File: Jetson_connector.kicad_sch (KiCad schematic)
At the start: 24 parts, among them IC2 AT24MAC402-MAHM-T, IC6 SN74AVC1T45DCKT, J2 QTH-060-01-L-D-A, U2 SN74AVC2T45DCUR

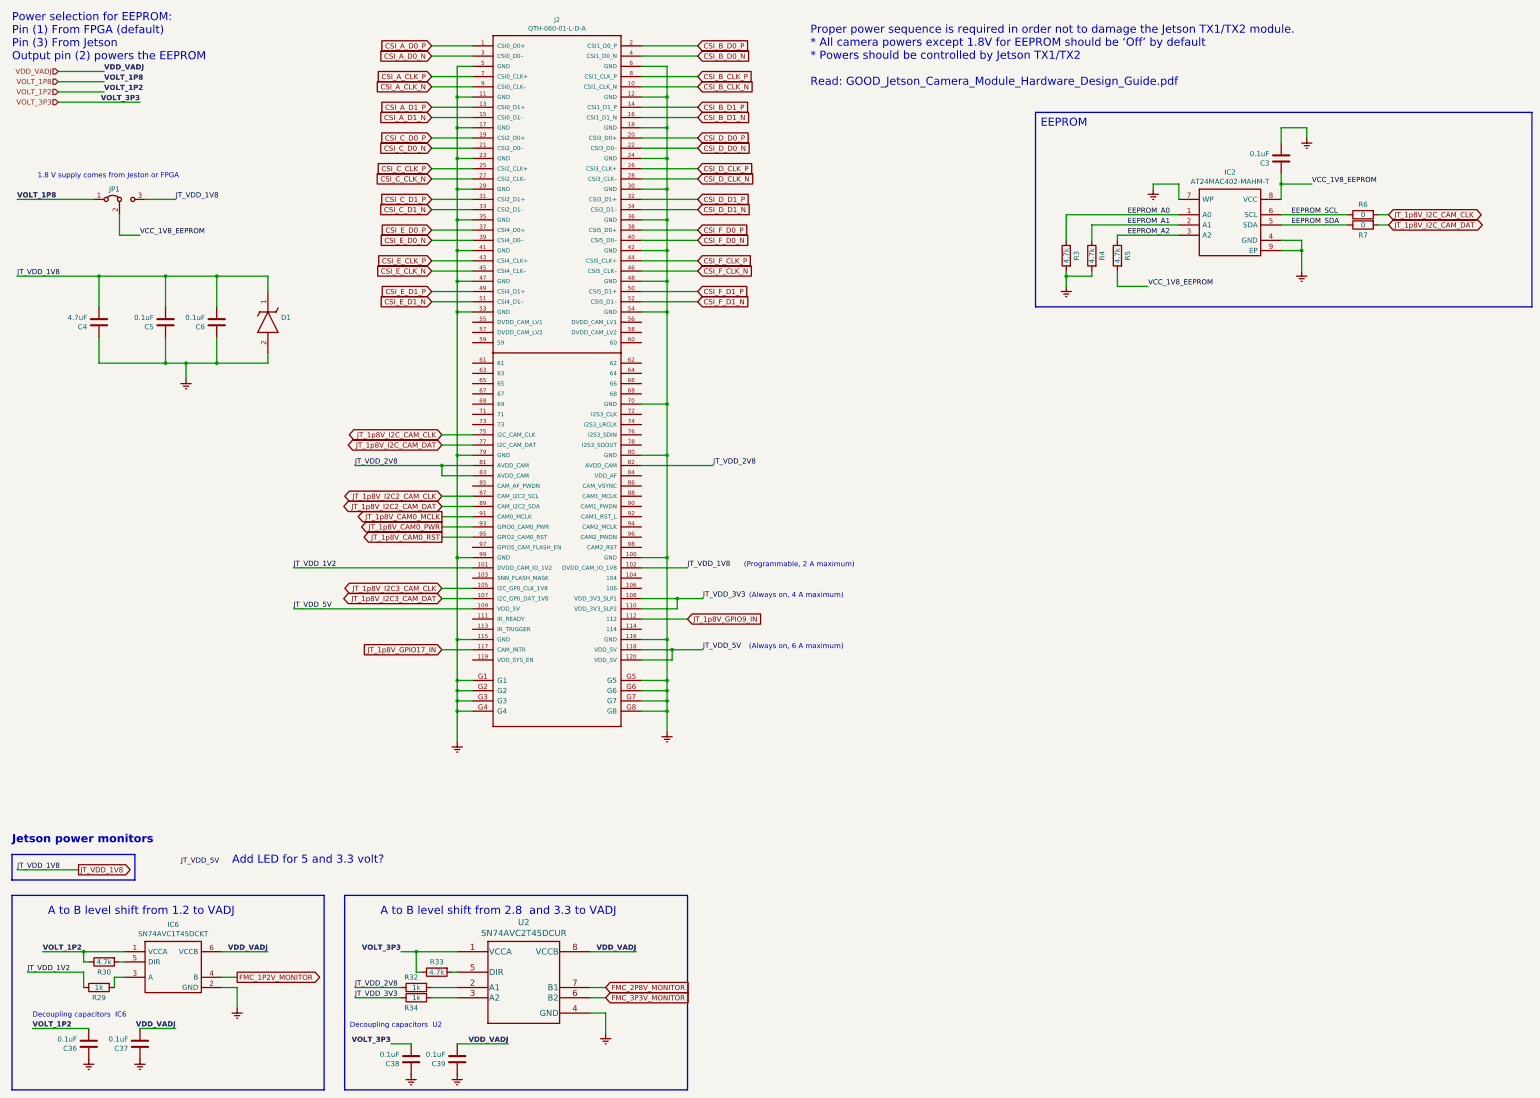
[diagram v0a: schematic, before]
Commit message: DRC, ERC OK
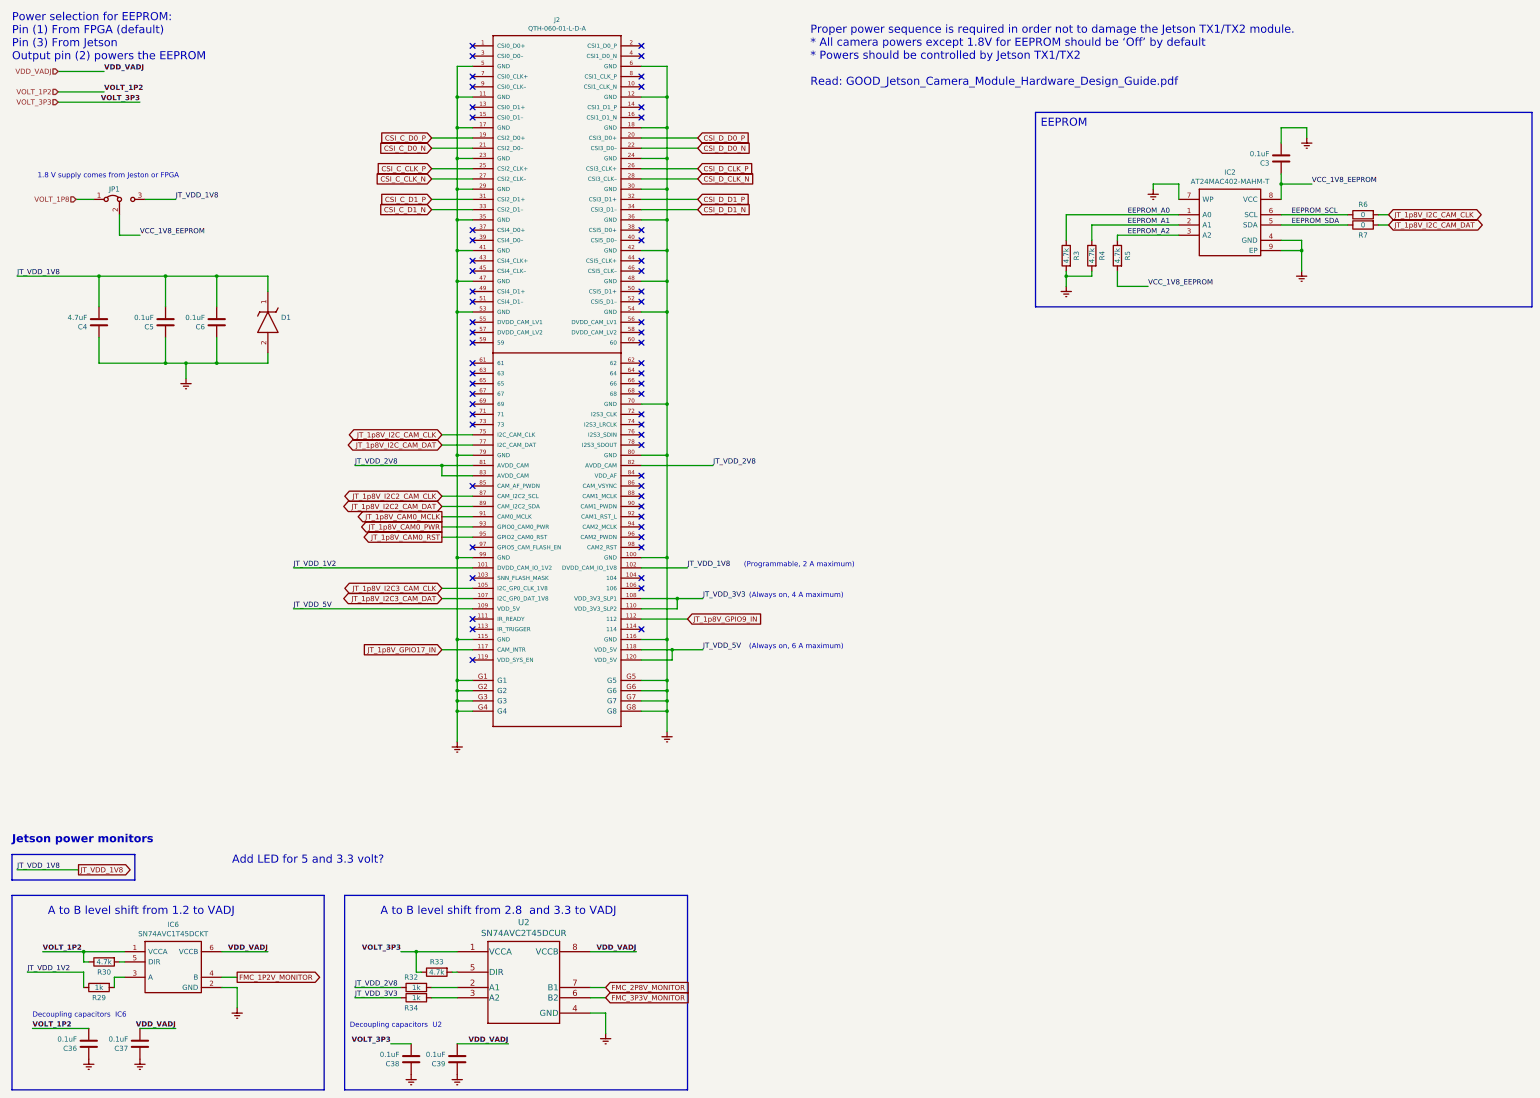
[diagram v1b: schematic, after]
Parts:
- D1: footprint Diodes_SMD:D_SOD-523 -> SODFL1608X70N
- IC6: footprint FMC_MIPI_v2_sym:SOT65P210X110-6N -> SOT65P210X110-6N
- JP1: symbol FMC_MIPI_v2-rescue:Jumper_3_Bridged12-Jumper -> FMC_MIPI_v2:Jumper_3_Bridged12-Jumper
- R29, R3, R30, R32, R33, R34, R4, R5, R6, R7: symbol FMC_MIPI_v2-rescue:R-Device -> FMC_MIPI_v2:R
- U2: footprint FMC_MIPI_v2_sym:SN74AVC2T45DCUR -> DCU8
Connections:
- net CSI_A_CLK_N: no longer names the net of J2.9 (CSI0_CLK–)
- net CSI_A_CLK_P: no longer names the net of J2.7 (CSI0_CLK+)
- net CSI_A_D0_N: no longer names the net of J2.3 (CSI0_D0–)
- net CSI_A_D0_P: no longer names the net of J2.1 (CSI0_D0+)
- net CSI_A_D1_N: no longer names the net of J2.15 (CSI0_D1–)
- net CSI_A_D1_P: no longer names the net of J2.13 (CSI0_D1+)
- net CSI_B_CLK_N: no longer names the net of J2.10 (CSI1_CLK_N)
- net CSI_B_CLK_P: no longer names the net of J2.8 (CSI1_CLK_P)
- net CSI_B_D0_N: no longer names the net of J2.4 (CSI1_D0_N)
- net CSI_B_D0_P: no longer names the net of J2.2 (CSI1_D0_P)
- net CSI_B_D1_N: no longer names the net of J2.16 (CSI1_D1_N)
- net CSI_B_D1_P: no longer names the net of J2.14 (CSI1_D1_P)
- net CSI_E_CLK_N: no longer names the net of J2.45 (CSI4_CLK–)
- net CSI_E_CLK_P: no longer names the net of J2.43 (CSI4_CLK+)
- net CSI_E_D0_N: no longer names the net of J2.39 (CSI4_D0–)
- net CSI_E_D0_P: no longer names the net of J2.37 (CSI4_D0+)
- net CSI_E_D1_N: no longer names the net of J2.51 (CSI4_D1–)
- net CSI_E_D1_P: no longer names the net of J2.49 (CSI4_D1+)
- net CSI_F_CLK_N: no longer names the net of J2.46 (CSI5_CLK–)
- net CSI_F_CLK_P: no longer names the net of J2.44 (CSI5_CLK+)
- net CSI_F_D0_N: no longer names the net of J2.40 (CSI5_D0–)
- net CSI_F_D0_P: no longer names the net of J2.38 (CSI5_D0+)
- net CSI_F_D1_N: no longer names the net of J2.52 (CSI5_D1–)
- net CSI_F_D1_P: no longer names the net of J2.50 (CSI5_D1+)
- removed net Earth: C3.2, C36.1, C37.1, C38.1, C39.1, C4.1, C5.1, C6.1, D1.2, IC2.4 (GND), IC2.7 (WP), IC2.9 (EP), IC6.2 (GND), J2.100 (GND), J2.11 (GND), J2.115 (GND), J2.116 (GND), J2.12 (GND), J2.17 (GND), J2.18 (GND), J2.23 (GND), J2.24 (GND), J2.29 (GND), J2.30 (GND), J2.35 (GND), J2.36 (GND), J2.41 (GND), J2.42 (GND), J2.47 (GND), J2.48 (GND), J2.5 (GND), J2.53 (GND), J2.54 (GND), J2.6 (GND), J2.70 (GND), J2.79 (GND), J2.80 (GND), J2.99 (GND), J2.G1, J2.G2, J2.G3, J2.G4, J2.G5, J2.G6, J2.G7, J2.G8, R3.2, R4.2, U2.4 (GND)
- new net: J2.100 (GND), J2.116 (GND), J2.12 (GND), J2.18 (GND), J2.24 (GND), J2.30 (GND), J2.36 (GND), J2.42 (GND), J2.48 (GND), J2.54 (GND), J2.6 (GND), J2.70 (GND), J2.80 (GND), J2.G5, J2.G6, J2.G7, J2.G8
- new net: J2.11 (GND), J2.115 (GND), J2.17 (GND), J2.23 (GND), J2.29 (GND), J2.35 (GND), J2.41 (GND), J2.47 (GND), J2.5 (GND), J2.53 (GND), J2.79 (GND), J2.99 (GND), J2.G1, J2.G2, J2.G3, J2.G4
- new net: C4.1, C5.1, C6.1, D1.2
- new net: IC2.4 (GND), IC2.9 (EP)
- new net: R3.2, R4.2
- no-connect marks 0 -> 62

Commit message: All warnings fixed
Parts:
- U2: footprint DCU8 -> FMC_MIPI_v2_sym:SN74AVC2T45DCUR
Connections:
- net Earth: now reaches J2.100 (GND), J2.116 (GND), J2.12 (GND), J2.18 (GND), J2.24 (GND), J2.30 (GND), J2.36 (GND), J2.42 (GND), J2.48 (GND), J2.54 (GND), J2.6 (GND), J2.70 (GND), J2.80 (GND), J2.G5, J2.G6, J2.G7, J2.G8
- net Earth: now also C3.2, C36.1, C37.1, C38.1, C39.1, C4.1, C5.1, C6.1, D1.2, IC2.4 (GND), IC2.7 (WP), IC2.9 (EP), IC6.2 (GND), J2.11 (GND), J2.115 (GND), J2.17 (GND), J2.23 (GND), J2.29 (GND), J2.35 (GND), J2.41 (GND), J2.47 (GND), J2.5 (GND), J2.53 (GND), J2.79 (GND), J2.99 (GND), J2.G1, J2.G2, J2.G3, J2.G4, R3.2, R4.2, U2.4 (GND)
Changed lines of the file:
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@@
       (effects (font (size 1.524 1.524)))
     )
-    (property "Footprint" "DCU8" (id 2) (at 142.24 242.57 0)
+    (property "Footprint" "FMC_MIPI_v2_sym:SN74AVC2T45DCUR" (id 2) (at 142.24 242.57 0)
       (effects (font (size 1.524 1.524)) hide)
     )

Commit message: JLCPCB BOM OK
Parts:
- C3, C36, C37, C38, C39, C5, C6: LCSC (none) -> C1525
- C4: LCSC (none) -> C1779; Part Number C2012X7R1H475K125AC -> CL21A475KAQNNNE
- D1: LCSC (none) -> C117557
- IC2, IC6, J2: LCSC (none) -> NeedToAsk
- JP1: LCSC (none) -> DnP; Part Number (none) -> 22-28-4033
- R29, R32, R34: value 1k -> 2.2k; LCSC (none) -> C17520; Part Number CRCW08051K00FKEAC -> (none)
- R3, R4, R5: LCSC (none) -> C17673
- R6, R7: LCSC (none) -> C17477; Part Number RC0805JR-070RL -> 0805W8F0000T5E
- U2: LCSC (none) -> C140318
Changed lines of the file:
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@@
       (effects (font (size 1.524 1.524)) hide)
+    )
+    (property "LCSC" "NeedToAsk" (id 4) (at 143.51 97.79 0)
+      (effects (font (size 1.27 1.27)) hide)
     )
     (pin "1")
@@
       (effects (font (size 1.27 1.27)) hide)
     )
-    (property "Datasheet" "~" (id 3) (at 41.91 59.69 0)
+    (property "Datasheet" "https://www.mouser.com/ProductDetail/Molex/22-28-4033?qs=d9fIA1aNikRRpuevshfBIQ%3D%3D" (id 3) (at 41.91 59.69 0)
+      (effects (font (size 1.27 1.27)) hide)
+    )
+    (property "Part Number" "22-28-4033" (id 4) (at 41.91 59.69 0)
+      (effects (font (size 1.27 1.27)) hide)
+    )
+    (property "LCSC" "DnP" (id 5) (at 41.91 59.69 0)
       (effects (font (size 1.27 1.27)) hide)
     )
@@
     (property "Manufacturer_Part_Number" "UCLAMP0501H.TCT" (id 9) (at 64.77 92.71 0)
       (effects (font (size 1.27 1.27)) (justify left bottom) hide)
+    )
+    (property "LCSC" "C117557" (id 10) (at 78.74 82.55 90)
+      (effects (font (size 1.27 1.27)) hide)
     )
     (pin "1")
@@
     (property "Manufacturer_Part_Number" "AT24MAC402-MAHM-T" (id 9) (at 326.39 73.66 0)
       (effects (font (size 1.27 1.27)) (justify left) hide)
+    )
+    (property "LCSC" "NeedToAsk" (id 10) (at 304.8 58.42 0)
+      (effects (font (size 1.27 1.27)) hide)
     )
     (pin "1")
@@
       (effects (font (size 1.27 1.27)) hide)
     )
+    (property "LCSC" "C1525" (id 7) (at 66.04 90.17 0)
+      (effects (font (size 1.27 1.27)) hide)
+    )
     (pin "1")
     (pin "2")
@@
       (effects (font (size 1.27 1.27)) hide)
     )
+    (property "LCSC" "C1525" (id 7) (at 53.34 90.17 0)
+      (effects (font (size 1.27 1.27)) hide)
+    )
     (pin "1")
     (pin "2")
@@
       (effects (font (size 1.27 1.27)) hide)
     )
-    (property "Datasheet" "https://www.mouser.com/ProductDetail/TDK/C2012X7R1H475K125AC?qs=P1JMDcb91o6brNyz9C%252BI3w%3D%3D" (id 3) (at 36.83 90.17 0)
-      (effects (font (size 1.27 1.27)) hide)
-    )
-    (property "Part Number" "C2012X7R1H475K125AC" (id 4) (at 36.83 90.17 0)
+    (property "Datasheet" "https://www.mouser.com/ProductDetail/Samsung-Electro-Mechanics/CL21A475KAQNNNE?qs=yOVawPpwOwkWIBpK%2Fbg0Aw%3D%3D" (id 3) (at 36.83 90.17 0)
+      (effects (font (size 1.27 1.27)) hide)
+    )
+    (property "Part Number" "CL21A475KAQNNNE" (id 4) (at 36.83 90.17 0)
       (effects (font (size 1.27 1.27)) hide)
     )
@@
     )
     (property "Voltage" "25V" (id 6) (at 36.83 90.17 0)
+      (effects (font (size 1.27 1.27)) hide)
+    )
+    (property "LCSC" "C1779" (id 7) (at 36.83 90.17 0)
       (effects (font (size 1.27 1.27)) hide)
     )
@@
       (effects (font (size 1.27 1.27)) hide)
     )
-    (property "Datasheet" "https://www.mouser.com/ProductDetail/YAGEO/RC0805JR-070RL?qs=3ldFlDWnkKyEhdaPjQHEFA%3D%3D" (id 3) (at 350.52 63.5 0)
+    (property "Datasheet" "https://www.mouser.com/ProductDetail/Royalohm/0805W8F0000T5E?qs=e8oIoAS2J1TZ0ecBNS6tzg%3D%3D" (id 3) (at 350.52 63.5 0)
       (effects (font (size 1.27 1.27)) hide)
     )
@@
       (effects (font (size 1.524 1.524)) hide)
     )
-    (property "Part Number" "RC0805JR-070RL" (id 6) (at 350.52 63.5 90)
-      (effects (font (size 1.524 1.524)) hide)
+    (property "Part Number" "0805W8F0000T5E" (id 6) (at 350.52 63.5 90)
+      (effects (font (size 1.524 1.524)) hide)
+    )
+    (property "LCSC" "C17477" (id 7) (at 388.62 198.12 90)
+      (effects (font (size 1.27 1.27)) hide)
     )
     (pin "1")
@@
       (effects (font (size 1.27 1.27)) hide)
     )
-    (property "Datasheet" "https://www.mouser.com/ProductDetail/YAGEO/RC0805JR-070RL?qs=3ldFlDWnkKyEhdaPjQHEFA%3D%3D" (id 3) (at 350.52 66.04 0)
+    (property "Datasheet" "https://www.mouser.com/ProductDetail/Royalohm/0805W8F0000T5E?qs=e8oIoAS2J1TZ0ecBNS6tzg%3D%3D" (id 3) (at 350.52 66.04 0)
       (effects (font (size 1.27 1.27)) hide)
     )
@@
       (effects (font (size 1.524 1.524)) hide)
     )
-    (property "Part Number" "RC0805JR-070RL" (id 6) (at 350.52 66.04 90)
-      (effects (font (size 1.524 1.524)) hide)
+    (property "Part Number" "0805W8F0000T5E" (id 6) (at 350.52 66.04 90)
+      (effects (font (size 1.524 1.524)) hide)
+    )
+    (property "LCSC" "C17477" (id 7) (at 388.62 198.12 90)
+      (effects (font (size 1.27 1.27)) hide)
     )
     (pin "1")
@@
     )
     (property "Voltage" "25V" (id 6) (at 330.2 49.53 0)
+      (effects (font (size 1.27 1.27)) hide)
+    )
+    (property "LCSC" "C1525" (id 7) (at 330.2 49.53 0)
       (effects (font (size 1.27 1.27)) hide)
     )
@@
       (effects (font (size 1.524 1.524)) hide)
     )
+    (property "LCSC" "C17673" (id 7) (at 276.86 73.66 90)
+      (effects (font (size 1.27 1.27)) hide)
+    )
     (pin "1")
     (pin "2")
@@
       (effects (font (size 1.524 1.524)) hide)
     )
+    (property "LCSC" "C17673" (id 7) (at 283.21 73.66 90)
+      (effects (font (size 1.27 1.27)) hide)
+    )
     (pin "1")
     (pin "2")
@@
       (effects (font (size 1.524 1.524)) hide)
     )
+    (property "LCSC" "C17673" (id 7) (at 289.56 73.66 90)
+      (effects (font (size 1.27 1.27)) hide)
+    )
     (pin "1")
     (pin "2")
@@
     (property "Manufacturer_Part_Number" "SN74AVC1T45DCKT" (id 9) (at 63.5 261.62 0)
       (effects (font (size 1.27 1.27)) (justify left) hide)
+    )
+    (property "LCSC" "NeedToAsk" (id 10) (at 39.37 246.38 0)
+      (effects (font (size 1.27 1.27)) hide)
     )
     (pin "1")
@@
     (in_bom yes) (on_board yes)
     (property "Reference" "R29" (id 0) (at 36.83 257.81 90))
-    (property "Value" "1k" (id 1) (at 36.83 255.27 90))
+    (property "Value" "2.2k" (id 1) (at 36.83 255.27 90))
     (property "Footprint" "Resistors_SMD:R_0805" (id 2) (at 36.83 253.492 90)
       (effects (font (size 1.27 1.27)) hide)
     )
-    (property "Datasheet" "https://www.mouser.com/ProductDetail/Vishay-Dale/CRCW08051K00FKEAC?qs=CZ6xfwOSLTXmQIgaYvN%2FBA%3D%3D" (id 3) (at 36.83 255.27 0)
+    (property "Datasheet" "" (id 3) (at 36.83 255.27 0)
       (effects (font (size 1.27 1.27)) hide)
     )
@@
       (effects (font (size 1.524 1.524)) hide)
     )
-    (property "Part Number" "CRCW08051K00FKEAC" (id 6) (at 36.83 255.27 90)
-      (effects (font (size 1.524 1.524)) hide)
+    (property "Part Number" "" (id 6) (at 36.83 255.27 90)
+      (effects (font (size 1.524 1.524)) hide)
+    )
+    (property "LCSC" "C17520" (id 7) (at 36.83 255.27 90)
+      (effects (font (size 1.27 1.27)) hide)
     )
     (pin "1")
@@
       (effects (font (size 1.27 1.27)) hide)
     )
+    (property "LCSC" "C1525" (id 7) (at 66.04 90.17 0)
+      (effects (font (size 1.27 1.27)) hide)
+    )
     (pin "1")
     (pin "2")
@@
     )
     (property "Voltage" "25V" (id 6) (at 46.99 269.24 0)
+      (effects (font (size 1.27 1.27)) hide)
+    )
+    (property "LCSC" "C1525" (id 7) (at 66.04 90.17 0)
       (effects (font (size 1.27 1.27)) hide)
     )
@@
     (in_bom yes) (on_board yes)
     (property "Reference" "R32" (id 0) (at 114.3 252.73 90))
-    (property "Value" "1k" (id 1) (at 115.57 255.27 90))
+    (property "Value" "2.2k" (id 1) (at 115.57 255.27 90))
     (property "Footprint" "Resistors_SMD:R_0805" (id 2) (at 115.57 253.492 90)
       (effects (font (size 1.27 1.27)) hide)
     )
-    (property "Datasheet" "https://www.mouser.com/ProductDetail/Vishay-Dale/CRCW08051K00FKEAC?qs=CZ6xfwOSLTXmQIgaYvN%2FBA%3D%3D" (id 3) (at 115.57 255.27 0)
+    (property "Datasheet" "" (id 3) (at 115.57 255.27 0)
       (effects (font (size 1.27 1.27)) hide)
     )
@@
       (effects (font (size 1.524 1.524)) hide)
     )
-    (property "Part Number" "CRCW08051K00FKEAC" (id 6) (at 115.57 255.27 90)
-      (effects (font (size 1.524 1.524)) hide)
+    (property "Part Number" "" (id 6) (at 115.57 255.27 90)
+      (effects (font (size 1.524 1.524)) hide)
+    )
+    (property "LCSC" "C17520" (id 7) (at 115.57 255.27 90)
+      (effects (font (size 1.27 1.27)) hide)
     )
     (pin "1")
@@
       (effects (font (size 1.27 1.27)) hide)
     )
+    (property "LCSC" "C1525" (id 7) (at 66.04 90.17 0)
+      (effects (font (size 1.27 1.27)) hide)
+    )
     (pin "1")
     (pin "2")
@@
     )
     (property "Voltage" "25V" (id 6) (at 125.73 273.05 0)
+      (effects (font (size 1.27 1.27)) hide)
+    )
+    (property "LCSC" "C1525" (id 7) (at 66.04 90.17 0)
       (effects (font (size 1.27 1.27)) hide)
     )
@@
     (property "Datasheet" "https://www.mouser.co.il/ProductDetail/Texas-Instruments/SN74AVC2T45DCUR?qs=gb35HGp1gQKZ06dJk1oX8w%3D%3D" (id 3) (at 142.24 241.7826 0)
       (effects (font (size 1.524 1.524)) hide)
+    )
+    (property "LCSC" "C140318" (id 4) (at 125.73 248.92 0)
+      (effects (font (size 1.27 1.27)) hide)
     )
     (pin "1")
@@
     (in_bom yes) (on_board yes)
     (property "Reference" "R34" (id 0) (at 114.3 260.35 90))
-    (property "Value" "1k" (id 1) (at 115.57 257.81 90))
+    (property "Value" "2.2k" (id 1) (at 115.57 257.81 90))
     (property "Footprint" "Resistors_SMD:R_0805" (id 2) (at 115.57 256.032 90)
       (effects (font (size 1.27 1.27)) hide)
     )
-    (property "Datasheet" "https://www.mouser.com/ProductDetail/Vishay-Dale/CRCW08051K00FKEAC?qs=CZ6xfwOSLTXmQIgaYvN%2FBA%3D%3D" (id 3) (at 115.57 257.81 0)
+    (property "Datasheet" "" (id 3) (at 115.57 257.81 0)
       (effects (font (size 1.27 1.27)) hide)
     )
@@
       (effects (font (size 1.524 1.524)) hide)
     )
-    (property "Part Number" "CRCW08051K00FKEAC" (id 6) (at 115.57 257.81 90)
-      (effects (font (size 1.524 1.524)) hide)
-    )
-    (pin "1")
+    (property "Part Number" "" (id 6) (at 115.57 257.81 90)
+      (effects (font (size 1.524 1.524)) hide)
+    )
+    (property "LCSC" "C17520" (id 7) (at 115.57 257.81 90)
+      (effects (font (size 1.27 1.27)) hide)
+    )
+    (pin "1")

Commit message: Generated BOM, before Gerbers generation
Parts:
- IC2: LCSC NeedToAsk -> C2061210
- IC6: LCSC NeedToAsk -> C2677669
- J2: LCSC NeedToAsk -> C3640977
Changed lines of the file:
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@@
       (effects (font (size 1.524 1.524)) hide)
     )
-    (property "LCSC" "NeedToAsk" (id 4) (at 143.51 97.79 0)
+    (property "LCSC" "C3640977" (id 4) (at 143.51 97.79 0)
       (effects (font (size 1.27 1.27)) hide)
     )
@@
       (effects (font (size 1.27 1.27)) (justify left) hide)
     )
-    (property "LCSC" "NeedToAsk" (id 10) (at 304.8 58.42 0)
+    (property "LCSC" "C2061210" (id 10) (at 304.8 58.42 0)
       (effects (font (size 1.27 1.27)) hide)
     )
@@
       (effects (font (size 1.27 1.27)) (justify left) hide)
     )
-    (property "LCSC" "NeedToAsk" (id 10) (at 39.37 246.38 0)
-      (effects (font (size 1.27 1.27)) hide)
-    )
+    (property "LCSC" "C2677669" (id 10) (at 39.37 246.38 0)
+      (effects (font (size 1.27 1.27)) hide)
+    )
